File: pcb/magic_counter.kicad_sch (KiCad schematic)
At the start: 16 parts, among them J1 ISP-Port, J2 Serial Out, SW1 Random, U1 ATmega32A-P, Y1 Crystal

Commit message: new parts and stuff
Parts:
- added J10: Barrel_Jack_Switch, Connector_BarrelJack:BarrelJack_Horizontal, symbol Connector:Barrel_Jack_Switch
- added J11: Screw_Terminal_01x02, TerminalBlock_Phoenix:TerminalBlock_Phoenix_PT-1,5-2-3.5-H_1x02_P3.50mm_Horizontal, symbol Connector:Screw_Terminal_01x02
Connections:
- net +5V: now also J10.1, J11.1 (Pin_1)
- net GND: now also J10.2, J10.3, J11.2 (Pin_2)
- net PD4: now reaches U1.18 (PD4)
- net PD5: now reaches U1.19 (PD5)
- net PD6: now reaches U1.20 (PD6)
- net PC4: now reaches U1.26 (PC4)
- net PC5: now reaches U1.27 (PC5)
- net PC6: now reaches U1.28 (PC6)
- net PC7: now reaches U1.29 (PC7)
- net PA4: no longer names the net of U1.36 (PA4)
- net PA5: no longer names the net of U1.35 (PA5)
- net PA6: no longer names the net of U1.34 (PA6)
- net PA7: no longer names the net of U1.33 (PA7)
- no-connect marks 0 -> 9
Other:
- added sheet Phase Switch (phases.kicad_sch)

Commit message: new routes
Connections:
- net RX: now also J2.3 (Pin_3); no longer J2.2 (Pin_2)
- net TX: now also J2.2 (Pin_2); no longer J2.3 (Pin_3)
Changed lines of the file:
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@@
     (effects (font (size 1.27 1.27)) (justify left bottom))
   )
-  (label "TX" (at 225.552 137.16 0)
+  (label "TX" (at 225.552 139.7 0)
     (effects (font (size 1.27 1.27)) (justify left bottom))
   )
@@
     (effects (font (size 1.27 1.27)) (justify right bottom))
   )
-  (label "RX" (at 225.552 139.7 0)
+  (label "RX" (at 225.552 137.16 0)
     (effects (font (size 1.27 1.27)) (justify left bottom))
   )

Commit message: layout changes
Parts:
- added H5, H6: MountingHole_Pad, MountingHole:MountingHole_3.2mm_M3_DIN965_Pad, symbol Mechanical:MountingHole_Pad
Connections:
- net GND: now also H5.1, H6.1
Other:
- moved on the sheet: H1, H2, H3, H4

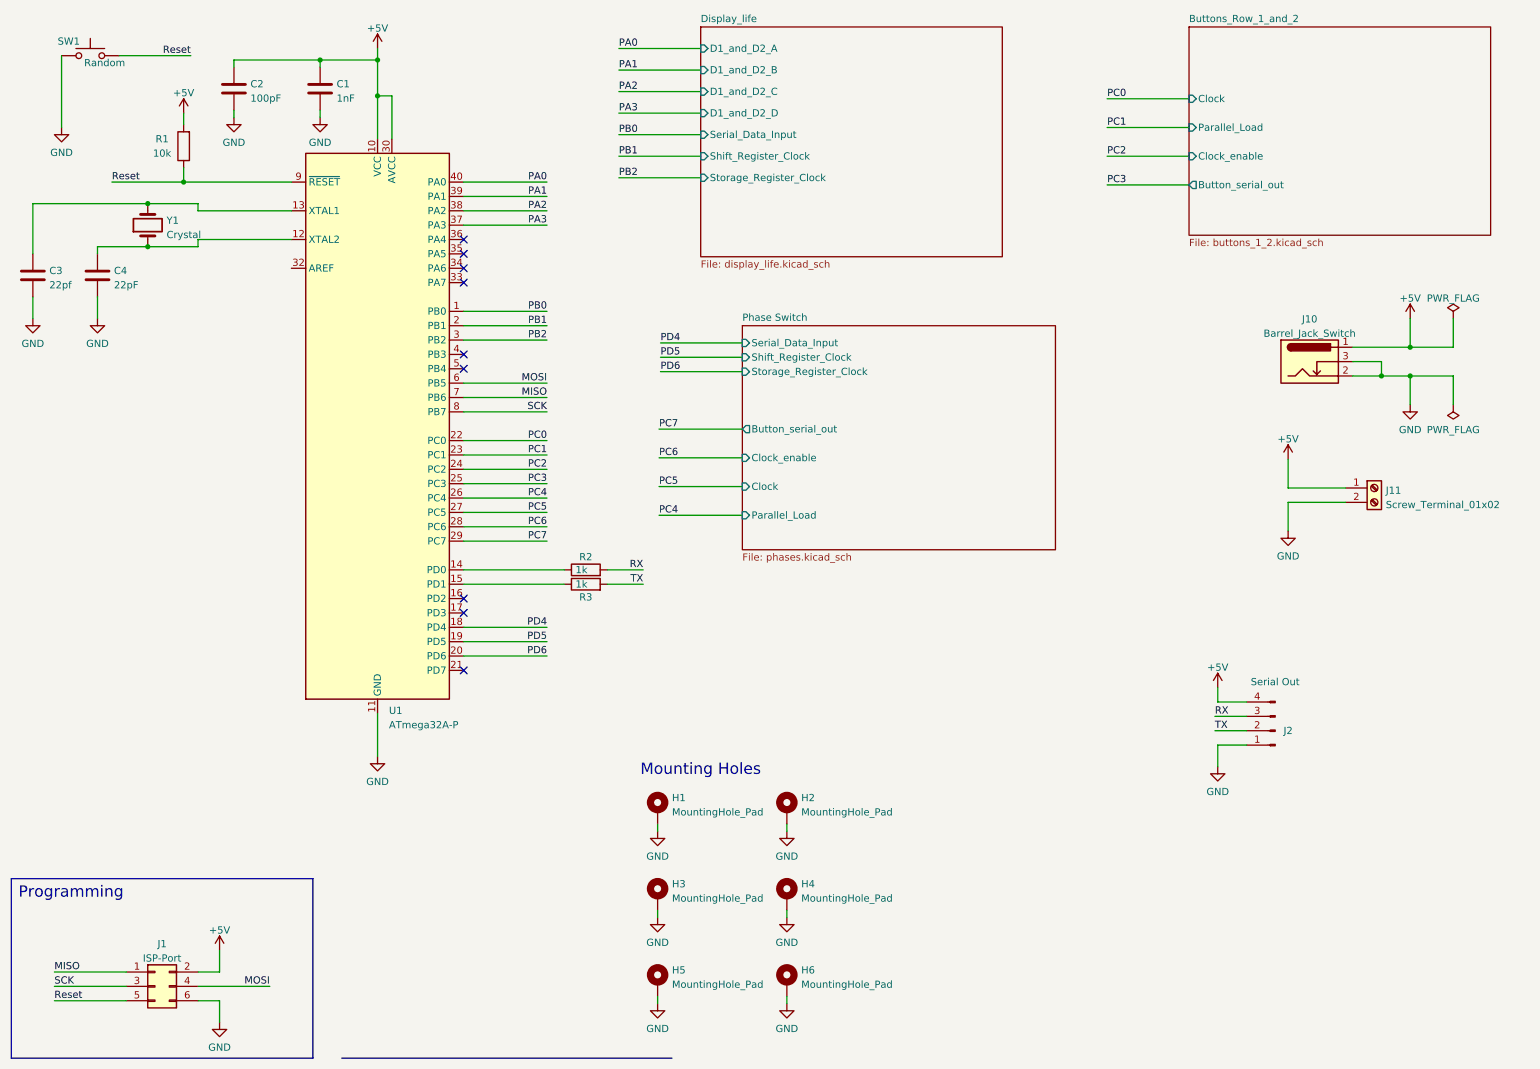
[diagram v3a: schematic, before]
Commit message: moved crystal
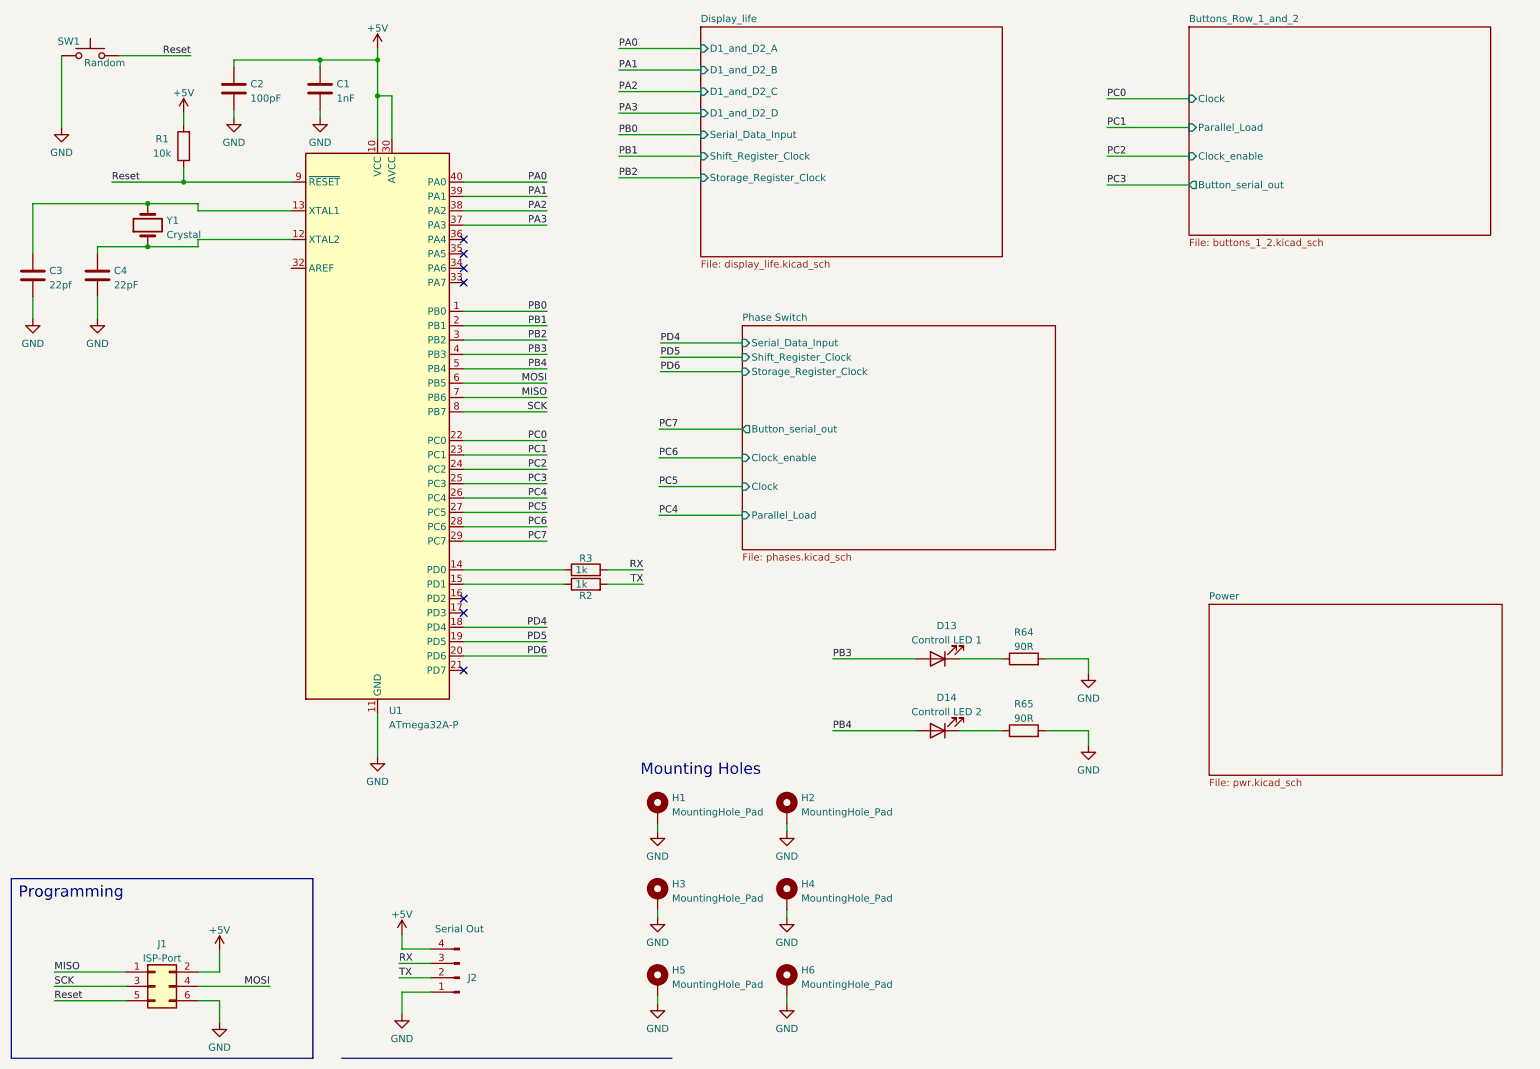
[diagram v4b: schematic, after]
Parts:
- removed J10: Barrel_Jack_Switch, Connector_BarrelJack:BarrelJack_Horizontal, symbol Connector:Barrel_Jack_Switch
- removed J11: Screw_Terminal_01x02, TerminalBlock_Phoenix:TerminalBlock_Phoenix_PT-1,5-2-3.5-H_1x02_P3.50mm_Horizontal, symbol Connector:Screw_Terminal_01x02
- added D13: Controll LED 1, LED_THT:LED_D5.0mm, symbol Device:LED
- added D14: Controll LED 2, LED_THT:LED_D5.0mm, symbol Device:LED
- added R64, R65: 90R, Resistor_THT:R_Axial_DIN0207_L6.3mm_D2.5mm_P7.62mm_Horizontal, symbol Device:R
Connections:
- net GND: now also R64.2, R65.2
- net RX: now also R3.2; no longer R2.2
- net TX: now also R2.2; no longer R3.2
- net at R3.1: now also U1.14 (PD0); no longer U1.15 (PD1)
- net at R2.1: now also U1.15 (PD1); no longer U1.14 (PD0)
- net PB3: now reaches U1.4 (PB3)
- net PB3: now also D13.2 (A)
- net PB4: now reaches U1.5 (PB4)
- net PB4: now also D14.2 (A)
- new net: D14.1 (K), R65.1
- new net: D13.1 (K), R64.1
- no-connect marks 9 -> 7
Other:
- added sheet Power (pwr.kicad_sch)
- moved on the sheet: J2, R2, R3

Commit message: production gerber and new pictures
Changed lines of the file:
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@@
     )
   )
-  (sheet (at 224.536 117.348) (size 51.816 30.226) (fields_autoplaced)
+  (sheet (at 17.78 111.76) (size 25.4 35.56) (fields_autoplaced)
     (stroke (width 0.1524) (type solid) (color 0 0 0 0))
     (fill (color 0 0 0 0.0000))
-    (property "Sheet name" "Power" (id 0) (at 224.536 116.6364 0)
+    (property "Sheet name" "Power" (id 0) (at 17.78 111.0484 0)
       (effects (font (size 1.27 1.27)) (justify left bottom))
     )
-    (property "Sheet file" "pwr.kicad_sch" (id 1) (at 224.536 148.1586 0)
+    (property "Sheet file" "pwr.kicad_sch" (id 1) (at 17.78 147.9046 0)
       (effects (font (size 1.27 1.27)) (justify left top))
     )

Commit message: new layout with usb
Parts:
- R1, R2, R3, R64, R65: footprint Resistor_THT:R_Axial_DIN0207_L6.3mm_D2.5mm_P7.62mm_Horizontal -> Resistor_THT:R_Axial_DIN0207_L6.3mm_D2.5mm_P10.16mm_Horizontal
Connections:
- net RX: now also J2.2 (Pin_2); no longer J2.3 (Pin_3)
- net TX: now also J2.3 (Pin_3); no longer J2.2 (Pin_2)
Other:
- sheet Power renamed Power and USB
- sheet Power and USB ports: added RXD, TXD; removed none

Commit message: pulldown to signals
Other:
- sheet Power and USB ports: added reset; removed none
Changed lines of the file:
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@@
+    (stroke (width 0) (type default) (color 0 0 0 0))
+  )
+  (wire (pts (xy 43.18 134.62) (xy 49.53 134.62))
     (stroke (width 0) (type default) (color 0 0 0 0))
   )
@@
   )
   (label "PB4" (at 107.442 75.692 180)
+    (effects (font (size 1.27 1.27)) (justify right bottom))
+  )
+  (label "Reset" (at 49.53 134.62 180)
     (effects (font (size 1.27 1.27)) (justify right bottom))
   )
@@
       (effects (font (size 1.27 1.27)) (justify right))
     )
+    (pin "reset" input (at 43.18 134.62 0)
+      (effects (font (size 1.27 1.27)) (justify right))
+    )
   )
   (sheet (at 220.98 15.24) (size 53.34 36.83) (fields_autoplaced)
@@
       (reference "#PWR0159") (unit 1) (value "GND") (footprint "")
     )
-    (path "/63ac5c74-ca82-4764-928a-a2069d691c7a/5592ee66-60d2-43e0-900e-190fc305c037"
-      (reference "#PWR0160") (unit 1) (value "GND") (footprint "")
-    )
-    (path "/63ac5c74-ca82-4764-928a-a2069d691c7a/6fd7d70c-f94e-47c7-8769-ed6073e6d225"
-      (reference "#PWR0161") (unit 1) (value "+5V") (footprint "")
-    )
-    (path "/63ac5c74-ca82-4764-928a-a2069d691c7a/86039871-6f8f-48b8-b7db-ca61c954b173"
-      (reference "#PWR0162") (unit 1) (value "+5V") (footprint "")
-    )
-    (path "/63ac5c74-ca82-4764-928a-a2069d691c7a/96629f02-37da-48bc-9a84-495417832fb0"
+    (path "/63ac5c74-ca82-4764-928a-a2069d691c7a/756b6221-cd9c-46b5-9685-bd1bc3e797c2"
+      (reference "#PWR0160") (unit 1) (value "+5V") (footprint "")
+    )
+    (path "/63ac5c74-ca82-4764-928a-a2069d691c7a/df95038e-c8e1-4e14-afb2-d1f5e0582539"
+      (reference "#PWR0161") (unit 1) (value "GND") (footprint "")
+    )
+    (path "/63ac5c74-ca82-4764-928a-a2069d691c7a/f58dd5a5-dabb-4e36-b7a6-75be1ced1f9e"
+      (reference "#PWR0162") (unit 1) (value "GND") (footprint "")
+    )
+    (path "/63ac5c74-ca82-4764-928a-a2069d691c7a/1ff1d071-6899-4bc4-9e41-35a47c929f6b"
       (reference "#PWR0163") (unit 1) (value "GND") (footprint "")
     )
@@
       (reference "#PWR0180") (unit 1) (value "GND") (footprint "")
     )
+    (path "/6c24aaa3-694e-4efb-a19c-b0182c95d014/10aea04b-be27-41a0-9554-412dc930900f"
+      (reference "#PWR0181") (unit 1) (value "GND") (footprint "")
+    )
+    (path "/6c24aaa3-694e-4efb-a19c-b0182c95d014/f4a08e07-8197-4ade-87e0-5f40bf807315"
+      (reference "#PWR0182") (unit 1) (value "GND") (footprint "")
+    )
+    (path "/6c24aaa3-694e-4efb-a19c-b0182c95d014/81c90061-c9de-4535-8cfe-103437e02d7c"
+      (reference "#PWR0183") (unit 1) (value "GND") (footprint "")
+    )
+    (path "/6c24aaa3-694e-4efb-a19c-b0182c95d014/e3954eca-c76e-442e-9f1d-36dfcd45c337"
+      (reference "#PWR0184") (unit 1) (value "GND") (footprint "")
+    )
+    (path "/6c24aaa3-694e-4efb-a19c-b0182c95d014/994780f5-edbb-4529-9f3b-bf1d3666c074"
+      (reference "#PWR0185") (unit 1) (value "GND") (footprint "")
+    )
+    (path "/6c24aaa3-694e-4efb-a19c-b0182c95d014/699a8f4b-36eb-4a6e-8f2e-8de9513a59d4"
+      (reference "#PWR0186") (unit 1) (value "GND") (footprint "")
+    )
+    (path "/6c24aaa3-694e-4efb-a19c-b0182c95d014/bf9922b8-c672-4b66-93fa-fac6c039880e"
+      (reference "#PWR0187") (unit 1) (value "GND") (footprint "")
+    )
+    (path "/6c24aaa3-694e-4efb-a19c-b0182c95d014/a879458e-9bca-4b06-b392-3f3991c1ee12"
+      (reference "#PWR0188") (unit 1) (value "GND") (footprint "")
+    )
+    (path "/6c24aaa3-694e-4efb-a19c-b0182c95d014/491090e4-8942-46e1-9a66-7d48cb5629a5"
+      (reference "#PWR0189") (unit 1) (value "GND") (footprint "")
+    )
+    (path "/6c24aaa3-694e-4efb-a19c-b0182c95d014/a10f4ed9-19cc-4876-b9df-36fd2c41c04d"
+      (reference "#PWR0190") (unit 1) (value "GND") (footprint "")
+    )
+    (path "/63ac5c74-ca82-4764-928a-a2069d691c7a/1a911b7c-28d8-49a3-9ddf-15818987112c"
+      (reference "#PWR0191") (unit 1) (value "GND") (footprint "")
+    )
+    (path "/63ac5c74-ca82-4764-928a-a2069d691c7a/32245cd8-c1c8-485c-bd5d-09db322c8e48"
+      (reference "#PWR0192") (unit 1) (value "GND") (footprint "")
+    )
+    (path "/63ac5c74-ca82-4764-928a-a2069d691c7a/6192d9dc-3f3c-40df-b2ec-b39bb554a143"
+      (reference "#PWR0193") (unit 1) (value "GND") (footprint "")
+    )
+    (path "/63ac5c74-ca82-4764-928a-a2069d691c7a/5605248c-0e0d-468b-8970-97c94ebdcb48"
+      (reference "#PWR0194") (unit 1) (value "GND") (footprint "")
+    )
+    (path "/63ac5c74-ca82-4764-928a-a2069d691c7a/7874bca9-865a-46ab-bf13-570c081a267c"
+      (reference "#PWR0195") (unit 1) (value "GND") (footprint "")
+    )
+    (path "/63ac5c74-ca82-4764-928a-a2069d691c7a/0edb6bb2-3dc0-425a-a2e5-2b7f40611d1f"
+      (reference "#PWR0196") (unit 1) (value "+5V") (footprint "")
+    )
     (path "/f876592a-053f-48ce-ba1b-3383cc8fcec7"
       (reference "C1") (unit 1) (value "1nF") (footprint "Capacitor_THT:C_Disc_D3.8mm_W2.6mm_P2.50mm")
@@
     )
     (path "/8ba761ec-fbbc-420c-b4ed-116ea8903523/17a86ac5-856f-4f34-8b92-86583403fac9"
-      (reference "C24") (unit 1) (value "10uF") (footprint "Capacitor_SMD:C_0805_2012Metric_Pad1.18x1.45mm_HandSolder")
+      (reference "C24") (unit 1) (value "22uF") (footprint "Capacitor_SMD:C_0805_2012Metric_Pad1.18x1.45mm_HandSolder")
     )
     (path "/63ac5c74-ca82-4764-928a-a2069d691c7a/792dde2c-8337-44b3-bef2-38e69e1dba8a"
@@
       (reference "R68") (unit 1) (value "1k") (footprint "Resistor_SMD:R_0805_2012Metric_Pad1.20x1.40mm_HandSolder")
     )
+    (path "/6c24aaa3-694e-4efb-a19c-b0182c95d014/546bea6c-f8cb-4a7d-9a50-6d2bcc5c44d6"
+      (reference "R69") (unit 1) (value "10k") (footprint "Resistor_THT:R_Axial_DIN0207_L6.3mm_D2.5mm_P10.16mm_Horizontal")
+    )
+    (path "/6c24aaa3-694e-4efb-a19c-b0182c95d014/ed44ec53-bea8-4f3a-b323-dbfbca80f4c4"
+      (reference "R70") (unit 1) (value "10k") (footprint "Resistor_THT:R_Axial_DIN0207_L6.3mm_D2.5mm_P10.16mm_Horizontal")
+    )
+    (path "/6c24aaa3-694e-4efb-a19c-b0182c95d014/891d565f-2a85-4fd9-9432-60a52dd4436e"
+      (reference "R71") (unit 1) (value "10k") (footprint "Resistor_THT:R_Axial_DIN0207_L6.3mm_D2.5mm_P10.16mm_Horizontal")
+    )
+    (path "/6c24aaa3-694e-4efb-a19c-b0182c95d014/1a6bebda-8d96-43eb-b5ab-75e2ed530104"
+      (reference "R72") (unit 1) (value "10k") (footprint "Resistor_THT:R_Axial_DIN0207_L6.3mm_D2.5mm_P10.16mm_Horizontal")
+    )
+    (path "/6c24aaa3-694e-4efb-a19c-b0182c95d014/1722f216-c0c0-452c-9ab5-8352fd96da83"
+      (reference "R73") (unit 1) (value "10k") (footprint "Resistor_THT:R_Axial_DIN0207_L6.3mm_D2.5mm_P10.16mm_Horizontal")
+    )
+    (path "/6c24aaa3-694e-4efb-a19c-b0182c95d014/d6e6c459-b2ca-44c7-88df-23c8eac8b8a4"
+      (reference "R74") (unit 1) (value "10k") (footprint "Resistor_THT:R_Axial_DIN0207_L6.3mm_D2.5mm_P10.16mm_Horizontal")
+    )
+    (path "/6c24aaa3-694e-4efb-a19c-b0182c95d014/21715d8c-52cd-4428-9bab-54242a727ffd"
+      (reference "R75") (unit 1) (value "10k") (footprint "Resistor_THT:R_Axial_DIN0207_L6.3mm_D2.5mm_P10.16mm_Horizontal")
+    )
+    (path "/6c24aaa3-694e-4efb-a19c-b0182c95d014/3d65fc45-7991-4642-878b-15b6e81066c6"
+      (reference "R76") (unit 1) (value "10k") (footprint "Resistor_THT:R_Axial_DIN0207_L6.3mm_D2.5mm_P10.16mm_Horizontal")
+    )
+    (path "/6c24aaa3-694e-4efb-a19c-b0182c95d014/966412b0-596b-43c7-9956-5e902059eb91"
+      (reference "R77") (unit 1) (value "10k") (footprint "Resistor_THT:R_Axial_DIN0207_L6.3mm_D2.5mm_P10.16mm_Horizontal")
+    )
+    (path "/6c24aaa3-694e-4efb-a19c-b0182c95d014/52d93f82-45eb-4656-a39a-ce3fda9c962a"
+      (reference "R78") (unit 1) (value "10k") (footprint "Resistor_THT:R_Axial_DIN0207_L6.3mm_D2.5mm_P10.16mm_Horizontal")
+    )
+    (path "/63ac5c74-ca82-4764-928a-a2069d691c7a/51ac04ab-b62c-4ba6-aafb-946897031d7a"
+      (reference "R79") (unit 1) (value "10k") (footprint "Resistor_THT:R_Axial_DIN0207_L6.3mm_D2.5mm_P10.16mm_Horizontal")
+    )
+    (path "/63ac5c74-ca82-4764-928a-a2069d691c7a/452cf89d-ca1f-4eec-abe6-a47e60468324"
+      (reference "R80") (unit 1) (value "10k") (footprint "Resistor_THT:R_Axial_DIN0207_L6.3mm_D2.5mm_P10.16mm_Horizontal")
+    )
+    (path "/63ac5c74-ca82-4764-928a-a2069d691c7a/539583f1-7086-41b1-b5f2-a4678504ea8a"
+      (reference "R81") (unit 1) (value "10k") (footprint "Resistor_THT:R_Axial_DIN0207_L6.3mm_D2.5mm_P10.16mm_Horizontal")
+    )
+    (path "/63ac5c74-ca82-4764-928a-a2069d691c7a/543577e7-5a2d-4e9d-8d13-a3ba6cc7199f"
+      (reference "R82") (unit 1) (value "10k") (footprint "Resistor_THT:R_Axial_DIN0207_L6.3mm_D2.5mm_P10.16mm_Horizontal")
+    )
+    (path "/63ac5c74-ca82-4764-928a-a2069d691c7a/d2e1549a-7ef5-4276-81f9-5a388e8e1748"
+      (reference "R83") (unit 1) (value "10k") (footprint "Resistor_THT:R_Axial_DIN0207_L6.3mm_D2.5mm_P10.16mm_Horizontal")
+    )
+    (path "/63ac5c74-ca82-4764-928a-a2069d691c7a/17275780-b53a-4584-895e-f0d85ea89dbc"
+      (reference "R84") (unit 1) (value "10k") (footprint "Resistor_THT:R_Axial_DIN0207_L6.3mm_D2.5mm_P10.16mm_Horizontal")
+    )
     (path "/efeeeed0-ec4d-43e9-b404-0b28a4668b90"
